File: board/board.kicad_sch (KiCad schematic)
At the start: 0 parts

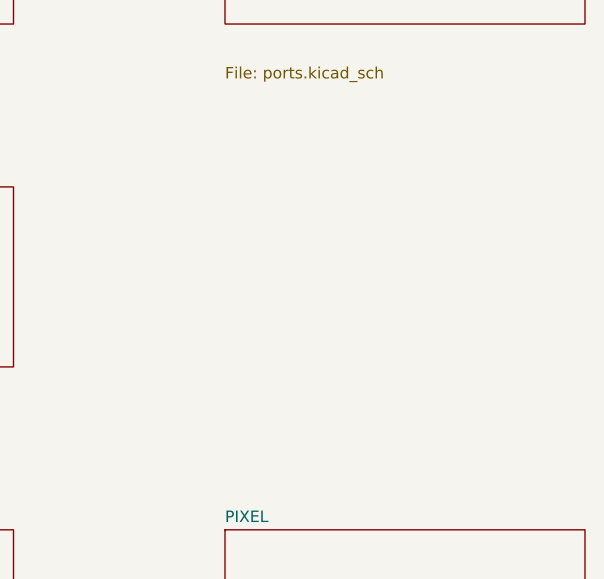
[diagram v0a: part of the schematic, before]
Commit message: add AUDIO_FIFO sheet; fix PORTS ~AUDIO_FIFO_EF onto pin 48
Co-Authored-By: Claude Fable 5.1 <noreply@anthropic.com>
Claude-Session: https://claude.ai/code/session_01NsFH8WNb3Tja14xUfwuyqj
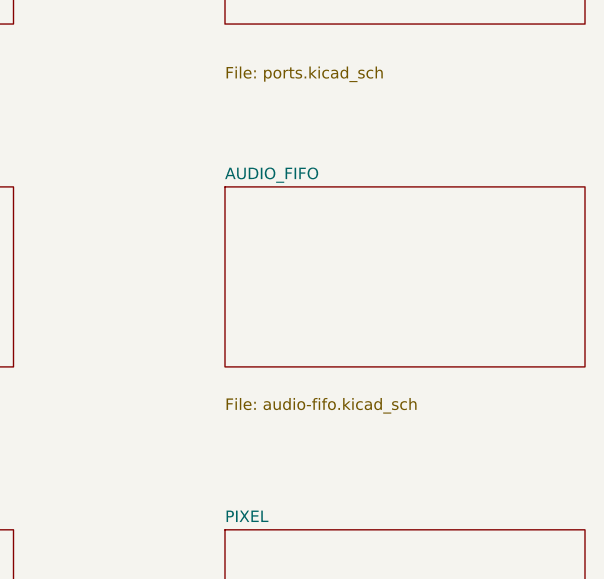
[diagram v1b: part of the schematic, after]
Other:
- added sheet AUDIO_FIFO (audio-fifo.kicad_sch)
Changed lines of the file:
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@@
+	)
+	(sheet
+		(at 215.9 63.5)
+		(size 40 20)
+		(exclude_from_sim no)
+		(in_bom yes)
+		(on_board yes)
+		(dnp no)
+		(fields_autoplaced yes)
+		(stroke
+			(width 0.1524)
+			(type solid)
+		)
+		(fill
+			(color 0 0 0 0.0000)
+		)
+		(property "Sheetname" "AUDIO_FIFO"
+			(at 215.9 62.7884 0)
+			(effects
+				(font
+					(size 1.27 1.27)
+				)
+				(justify left bottom)
+			)
+		)
+		(property "Sheetfile" "audio-fifo.kicad_sch"
+			(at 215.9 86.9446 0)
+			(effects
+				(font
+					(size 1.27 1.27)
+				)
+				(justify left top)
+			)
+		)
+		(instances
+			(project "board"
+				(path "/afefa398-9f39-4b22-97f8-dae9b102df0d"
+					(page "15")
+				)
+			)
+		)
 	)
 	(sheet

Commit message: add DEBUG_HEADER sheet (2x16 LogicAnalyzer V2 pinout); re-annotate AUDIO_FIFO
Co-Authored-By: Claude Fable 5.1 <noreply@anthropic.com>
Claude-Session: https://claude.ai/code/session_01NsFH8WNb3Tja14xUfwuyqj
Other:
- added sheet DEBUG_HEADER (debug-header.kicad_sch)
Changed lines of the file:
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@@
 	)
 	(embedded_fonts no)
+	(sheet
+		(at 152.4 138.43)
+		(size 40 20)
+		(exclude_from_sim no)
+		(in_bom yes)
+		(on_board yes)
+		(dnp no)
+		(fields_autoplaced yes)
+		(stroke
+			(width 0.1524)
+			(type solid)
+		)
+		(fill
+			(color 0 0 0 0.0000)
+		)
+		(property "Sheetname" "DEBUG_HEADER"
+			(at 152.4 137.7184 0)
+			(effects
+				(font
+					(size 1.27 1.27)
+				)
+				(justify left bottom)
+			)
+		)
+		(property "Sheetfile" "debug-header.kicad_sch"
+			(at 152.4 161.8746 0)
+			(effects
+				(font
+					(size 1.27 1.27)
+				)
+				(justify left top)
+			)
+		)
+		(instances
+			(project "board"
+				(path "/afefa398-9f39-4b22-97f8-dae9b102df0d"
+					(page "16")
+				)
+			)
+		)
+	)
 )
